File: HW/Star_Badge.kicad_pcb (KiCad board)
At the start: 2 copper layers, 180 x 171.6 mm, 55 parts, among them J1 AVR-ISP-6, J2 10118194-0001LF, Q1 Q_NMOS_DGS, Q2 Q_PMOS_DGS, U1 ATTINY861-15XD, U2 TPS613221ADBVT, U3 AP7363-33D-13, X1 Badgelife_sao_connector_v169b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, X2 Badgelife_sao_connector_v169b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, X3 Badgelife_sao_connector_v169b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

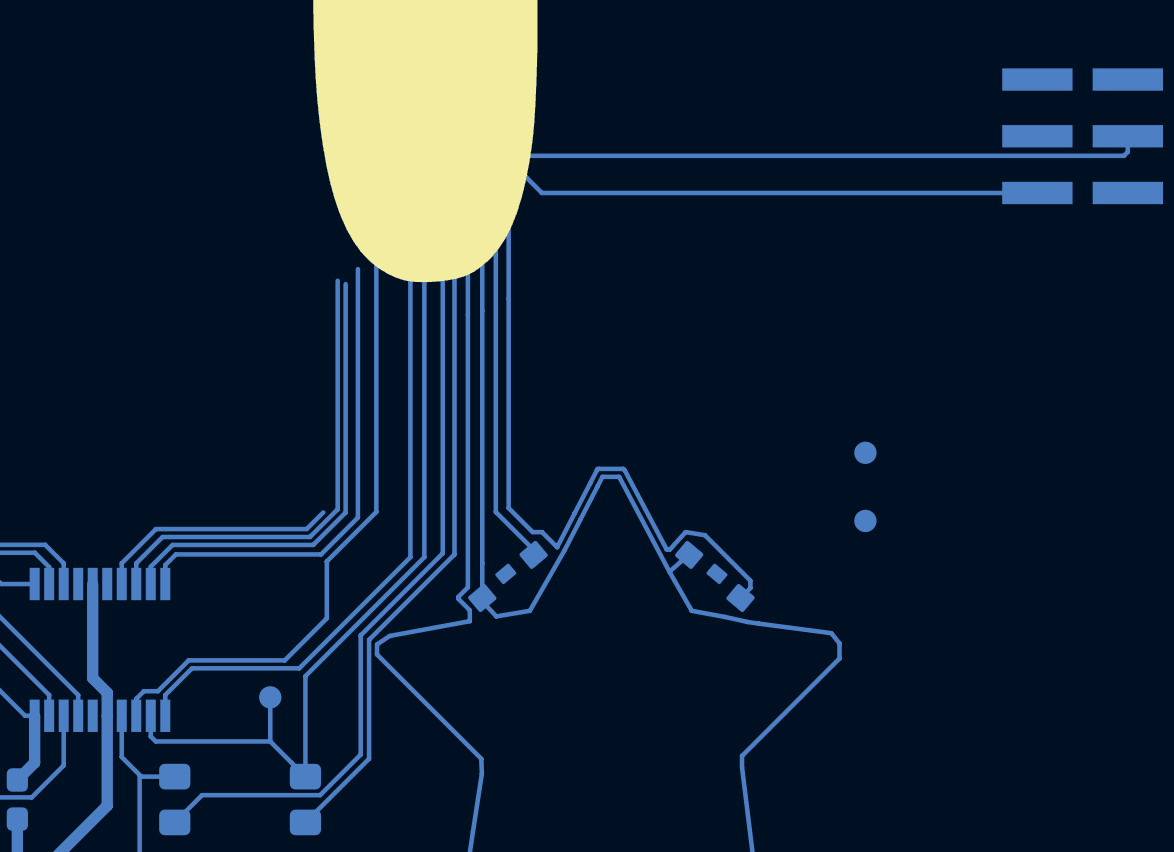
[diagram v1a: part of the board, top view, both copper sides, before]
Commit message: routed sclock to programming header
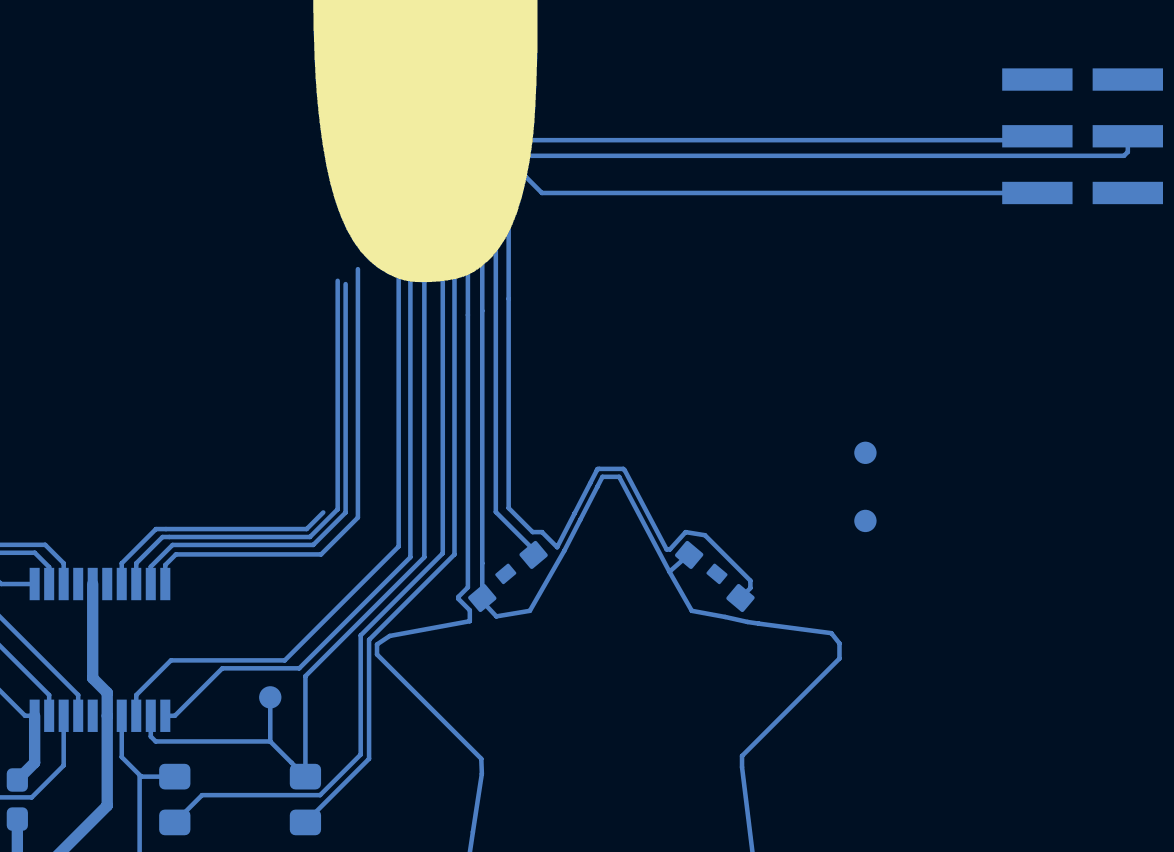
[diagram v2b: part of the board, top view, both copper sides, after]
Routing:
- net /SCL_SCK: track 28.5 -> 61.9 mm, vias 0 -> 2
- net /SDA_MOSI: track 65.3 -> 64.6 mm
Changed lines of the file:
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@@
     (thickness 1.6)
     (drawings 611)
-    (tracks 757)
+    (tracks 761)
     (zones 0)
     (modules 55)
@@
   (segment (start 99.675 134.268478) (end 100.325 134.918478) (width 0.508) (layer B.Cu) (net 15))
   (segment (start 99.675 130.05) (end 99.675 134.268478) (width 0.508) (layer B.Cu) (net 15))
-  (segment (start 101.967798 134.85) (end 102.593892 134.85) (width 0.2032) (layer B.Cu) (net 16))
-  (segment (start 101.625 135.95) (end 101.625 135.192798) (width 0.2032) (layer B.Cu) (net 16))
-  (segment (start 101.625 135.192798) (end 101.967798 134.85) (width 0.2032) (layer B.Cu) (net 16))
-  (segment (start 102.593892 134.85) (end 103.974502 133.46939) (width 0.2032) (layer B.Cu) (net 16))
-  (segment (start 103.974502 133.46939) (end 108.274794 133.46939) (width 0.2032) (layer B.Cu) (net 16))
-  (segment (start 108.274794 133.46939) (end 110.15817 131.586014) (width 0.2032) (layer B.Cu) (net 16))
-  (segment (start 110.15817 129.04183) (end 110.158171 129.038921) (width 0.2032) (layer B.Cu) (net 16))
-  (segment (start 110.15817 131.586014) (end 110.15817 129.04183) (width 0.2032) (layer B.Cu) (net 16))
-  (segment (start 110.158171 129.038921) (end 112.375 126.822092) (width 0.2032) (layer B.Cu) (net 16))
-  (segment (start 112.375 126.822092) (end 112.375 114.775) (width 0.2032) (layer B.Cu) (net 16))
-  (segment (start 102.925 135.0218) (end 104.1218 133.825) (width 0.2032) (layer B.Cu) (net 17))
-  (segment (start 102.925 135.95) (end 102.925 135.0218) (width 0.2032) (layer B.Cu) (net 17))
-  (segment (start 104.1218 133.825) (end 108.925 133.825) (width 0.2032) (layer B.Cu) (net 17))
-  (segment (start 108.925 133.825) (end 113.9 128.85) (width 0.2032) (layer B.Cu) (net 17))
-  (segment (start 113.9 128.85) (end 113.9 116.5) (width 0.2032) (layer B.Cu) (net 17))
-  (segment (start 113.9 116.5) (end 113.9 110.875) (width 0.2032) (layer B.Cu) (net 17))
-  (segment (start 113.9 110.875) (end 113.9 110.875) (width 0.2032) (layer B.Cu) (net 17))
-  (via (at 113.9 110.875) (size 0.4) (drill 0.3) (layers F.Cu B.Cu) (net 17))
-  (segment (start 113.9 110.875) (end 118.9 110.875) (width 0.2032) (layer F.Cu) (net 17))
+  (via (at 113.375 110.825) (size 0.4) (drill 0.3) (layers F.Cu B.Cu) (net 16))
+  (segment (start 113.375 111.107842) (end 113.375 110.825) (width 0.2032) (layer B.Cu) (net 16))
+  (segment (start 113.375 128.369184) (end 113.375 111.107842) (width 0.2032) (layer B.Cu) (net 16))
+  (segment (start 108.274794 133.46939) (end 113.375 128.369184) (width 0.2032) (layer B.Cu) (net 16))
+  (segment (start 103.17741 133.46939) (end 108.274794 133.46939) (width 0.2032) (layer B.Cu) (net 16))
+  (segment (start 101.625 135.95) (end 101.625 135.0218) (width 0.2032) (layer B.Cu) (net 16))
+  (segment (start 101.625 135.0218) (end 103.17741 133.46939) (width 0.2032) (layer B.Cu) (net 16))
+  (segment (start 113.375 110.825) (end 114.025 110.175) (width 0.2032) (layer F.Cu) (net 16))
+  (segment (start 114.025 110.175) (end 118.9 110.175) (width 0.2032) (layer F.Cu) (net 16))
+  (segment (start 118.9 110.175) (end 118.9 110.175) (width 0.2032) (layer F.Cu) (net 16))
+  (via (at 118.9 110.175) (size 0.4) (drill 0.3) (layers F.Cu B.Cu) (net 16))
+  (segment (start 141.8 110.175) (end 141.975 110) (width 0.2032) (layer B.Cu) (net 16))
+  (segment (start 118.9 110.175) (end 141.8 110.175) (width 0.2032) (layer B.Cu) (net 16))
   (segment (start 118.9 110.875) (end 118.9 110.875) (width 0.2032) (layer F.Cu) (net 17))
   (via (at 118.9 110.875) (size 0.4) (drill 0.3) (layers F.Cu B.Cu) (net 17))
@@
   (segment (start 145.8532 110.875) (end 146.025 110.7032) (width 0.2032) (layer B.Cu) (net 17))
   (segment (start 118.9 110.875) (end 145.8532 110.875) (width 0.2032) (layer B.Cu) (net 17))
+  (segment (start 118.9 110.875) (end 114.25 110.875) (width 0.2032) (layer F.Cu) (net 17))
+  (segment (start 105.4782 133.825) (end 108.925 133.825) (width 0.2032) (layer B.Cu) (net 17))
+  (via (at 113.9 111.225) (size 0.4) (drill 0.3) (layers F.Cu B.Cu) (net 17))
+  (segment (start 114.099999 111.025001) (end 113.9 111.225) (width 0.2032) (layer F.Cu) (net 17))
+  (segment (start 114.25 110.875) (end 114.099999 111.025001) (width 0.2032) (layer F.Cu) (net 17))
+  (segment (start 103.3532 135.95) (end 105.4782 133.825) (width 0.2032) (layer B.Cu) (net 17))
+  (segment (start 113.9 111.507842) (end 113.9 111.225) (width 0.2032) (layer B.Cu) (net 17))
+  (segment (start 113.9 128.85) (end 113.9 111.507842) (width 0.2032) (layer B.Cu) (net 17))
+  (segment (start 108.925 133.825) (end 113.9 128.85) (width 0.2032) (layer B.Cu) (net 17))
+  (segment (start 102.925 135.95) (end 103.3532 135.95) (width 0.2032) (layer B.Cu) (net 17))
   (segment (start 97.075 138.05) (end 96.3 138.825) (width 0.508) (layer B.Cu) (net 18))
   (segment (start 97.075 135.95) (end 97.075 138.05) (width 0.508) (layer B.Cu) (net 18))

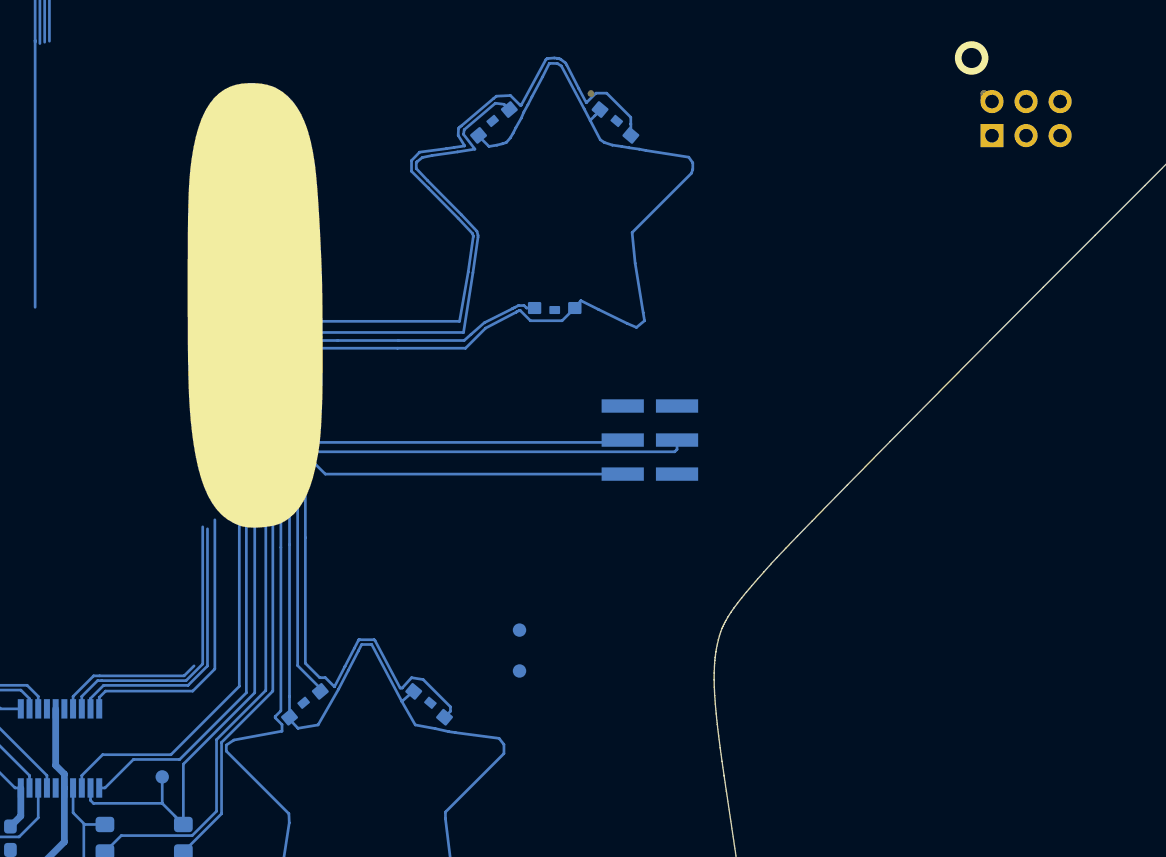
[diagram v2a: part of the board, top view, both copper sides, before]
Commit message: routed gpio pins to SOA 2
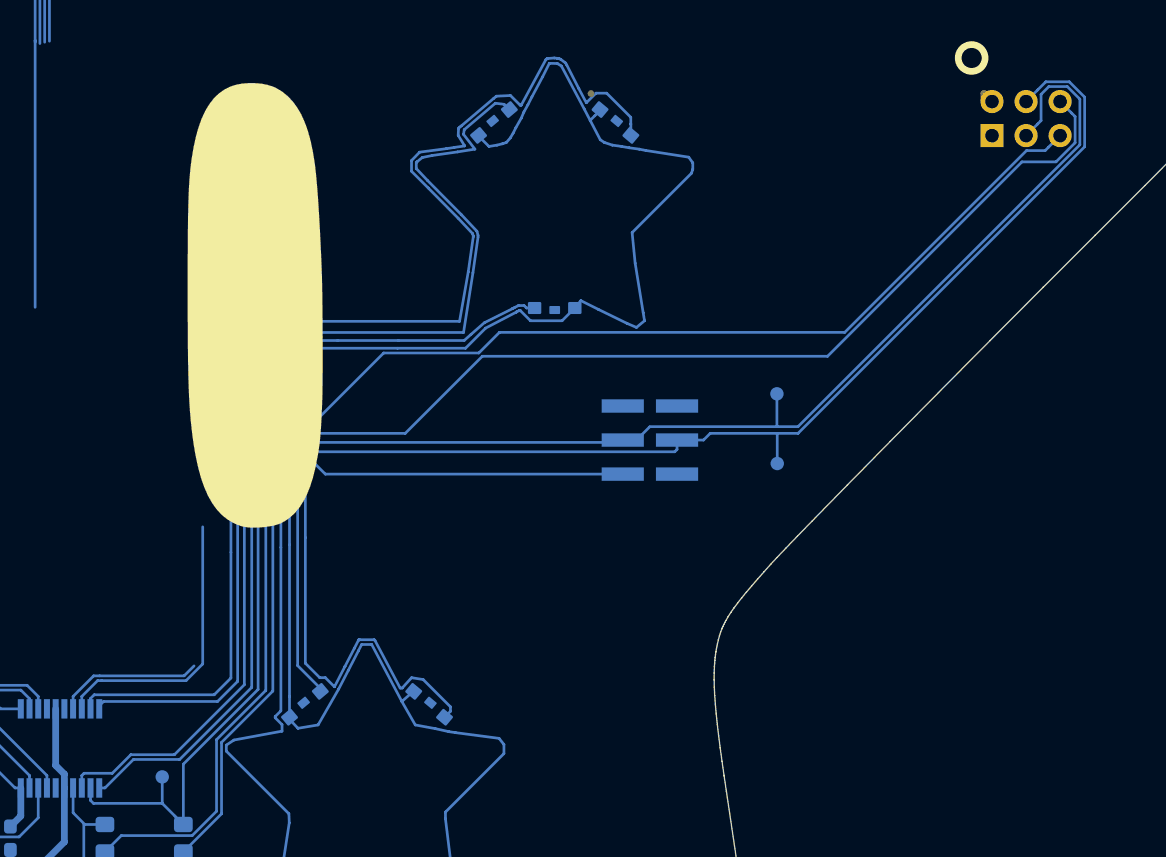
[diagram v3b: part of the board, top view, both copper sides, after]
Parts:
- moved TP2 26.1 mm to (153.5, 106.5)
- moved TP1 24.7 mm to (153.5, 111.8)
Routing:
- net /GPIO_1_1: track 21.5 -> 103.9 mm, vias 0 -> 2
- net /GPIO_1_2: track 20.7 -> 100.9 mm, vias 0 -> 2
- net /SCL_SCK: track 61.9 -> 118.0 mm
- net /SDA_MOSI: track 64.6 -> 114.2 mm

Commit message: More routing
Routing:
- net /GPIO_2_1: track 21.2 -> 124.9 mm, vias 0 -> 2
- net /EN_RGB1: track 66.3 -> 108.2 mm, vias 0 -> 2
- net /EN_RGB0: track 78.2 -> 103.1 mm, vias 0 -> 2

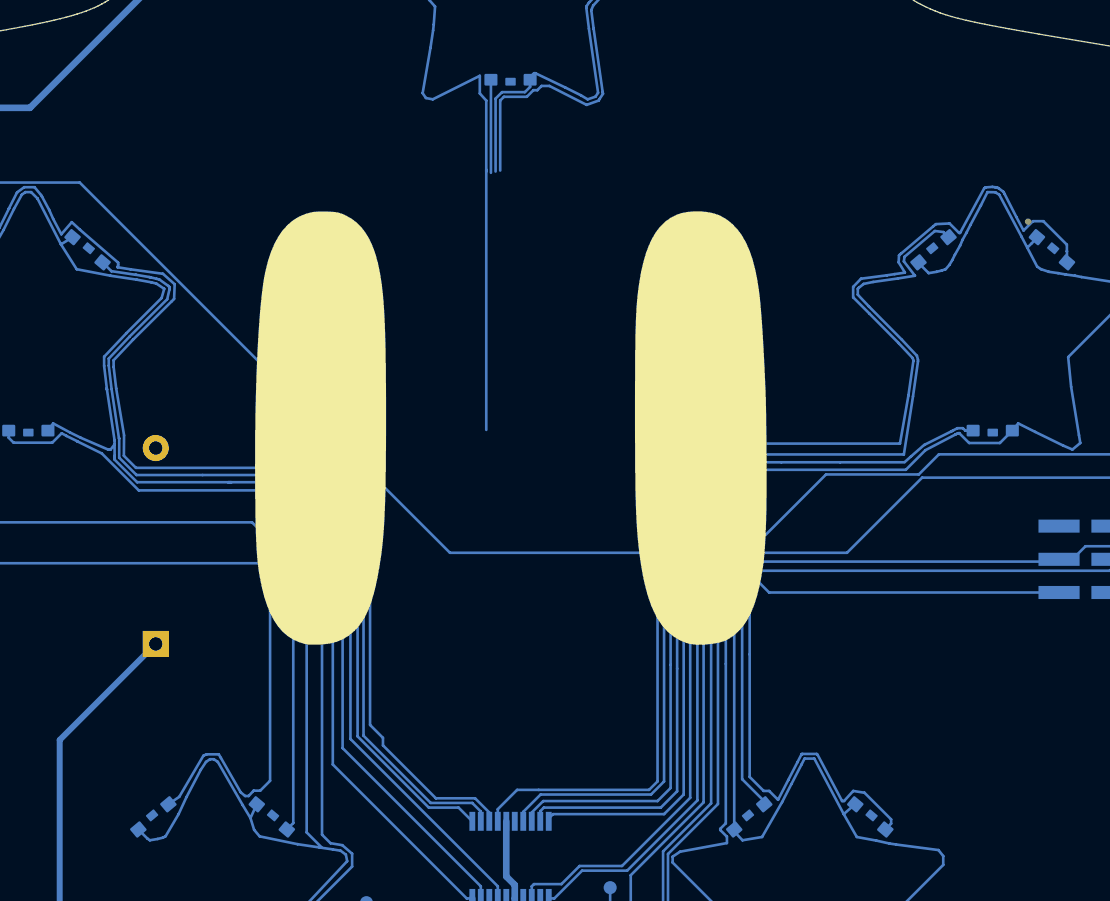
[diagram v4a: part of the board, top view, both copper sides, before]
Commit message: G_LED_BUS connected
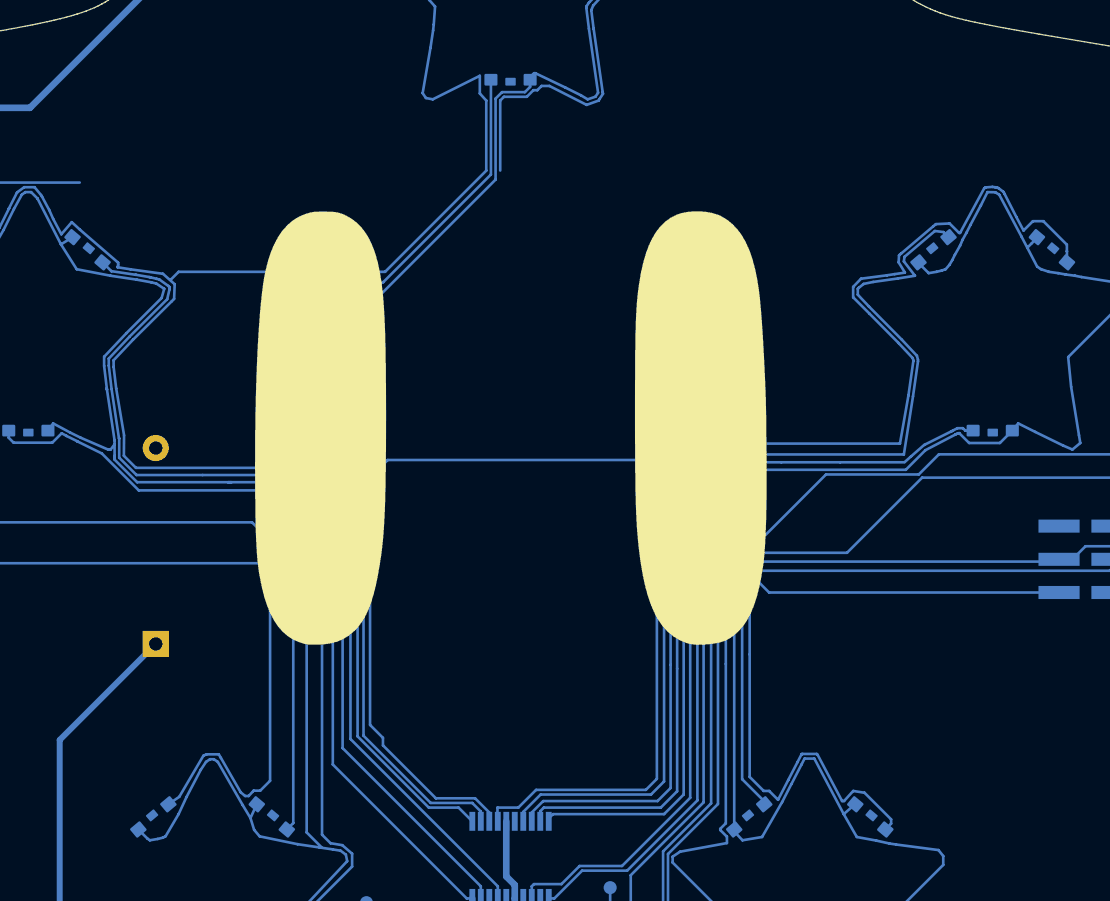
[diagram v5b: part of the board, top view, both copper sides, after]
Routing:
- net /GPIO_2_1: track 124.9 -> 69.7 mm
- net /G_LED_BUS: track 242.2 -> 286.4 mm, vias 6 -> 10
- net /B_LED_BUS: track 168.1 -> 179.9 mm, vias 2 -> 3
- net /EN_RGB2: track 85.8 -> 97.1 mm, vias 0 -> 1
- net /EN_RGB3: track 95.0 -> 89.3 mm
- net /~RESET: track 32.9 -> 36.6 mm
- net /EN_RGB1: track 108.2 -> 110.9 mm
